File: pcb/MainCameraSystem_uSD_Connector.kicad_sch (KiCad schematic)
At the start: 10 parts, among them J3 0472192001

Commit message: Removed series resistors for `uSD Connector` design block.
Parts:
- removed R11, R12, R13, R14, R15, R16: R_Small, Resistor_SMD:R_1206_3216Metric_Pad1.30x1.75mm_HandSolder, symbol Device:R_Small
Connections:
- net clock: now also J3.5 (CLK)
- net cmd: now also J3.3 (CMD)
- net data_0: now also J3.7 (DAT0)
- net data_1: now also J3.8 (DAT1)
- net data_2: now also J3.1 (DAT2)
- net data_3: now also J3.2 (DAT3/CD)
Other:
- note added: "uSD Connector (V7 : Removed series resistor)."
- note removed: "uSD Connector (V6 : Hierarchical labels)."

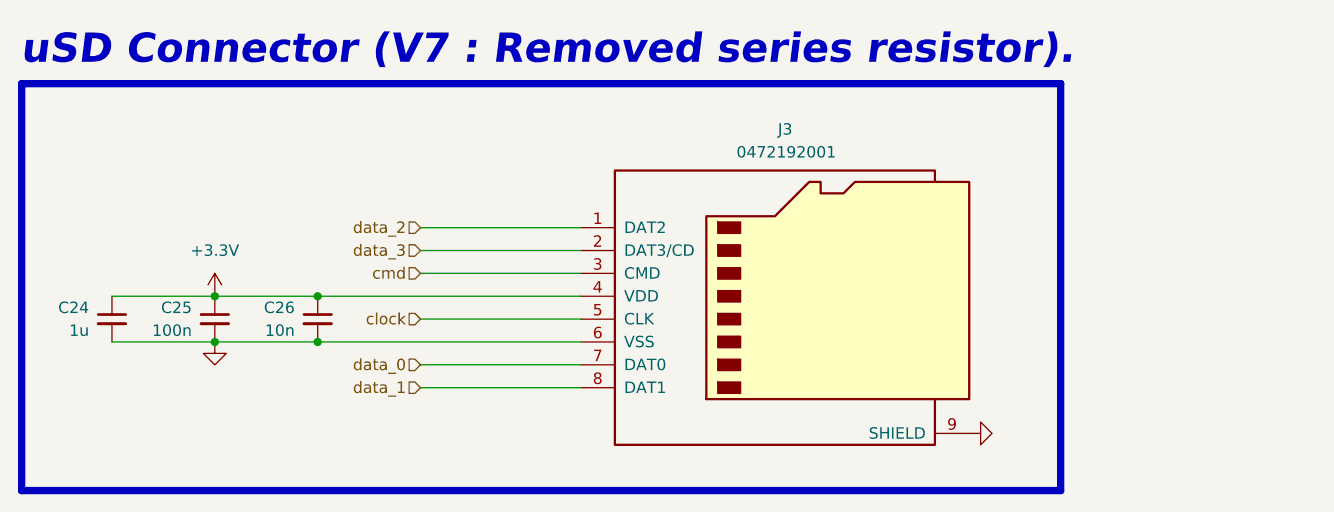
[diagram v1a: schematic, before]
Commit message: Fixing errata of missing pull-up resistors on `CMD` and `DAT0` lines of uSD connector.
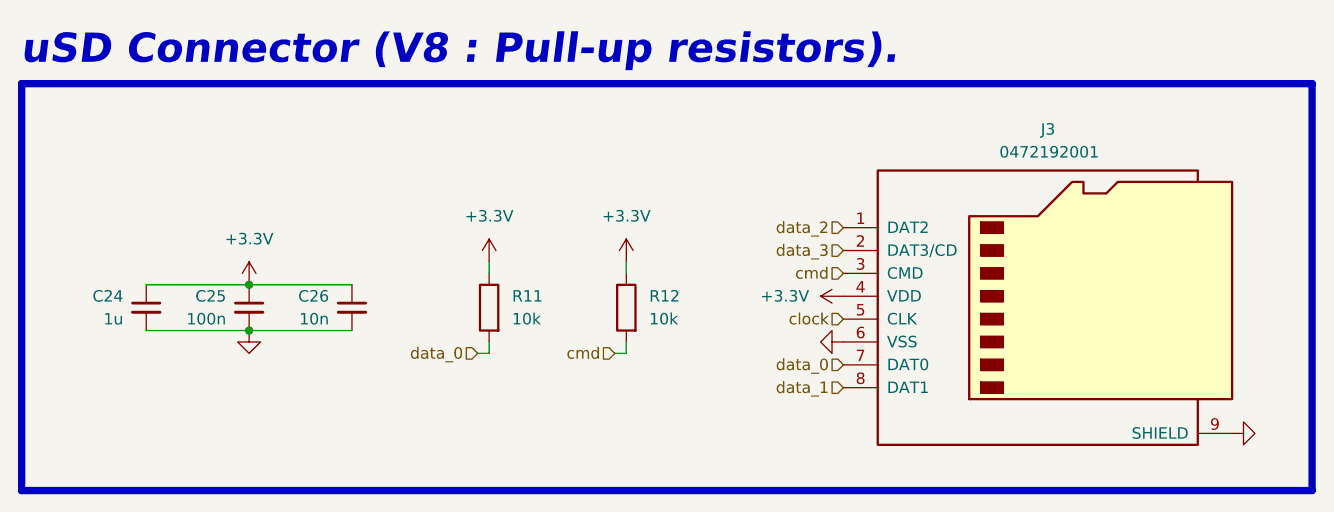
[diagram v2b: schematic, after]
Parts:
- added R11, R12: 10k, Resistor_SMD:R_1206_3216Metric_Pad1.30x1.75mm_HandSolder, symbol Device:R
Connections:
- net +3.3V: now also R11.1, R12.1
- net cmd: now also R12.2
- net data_0: now also R11.2
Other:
- note added: "uSD Connector (V8 : Pull-up resistors)."
- note removed: "uSD Connector (V7 : Removed series resistor)."
- moved on the sheet: C24, C25, C26, J3

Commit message: Laid out silkscreen and fixed schematic and PCB issues for `MainCameraSystem`.
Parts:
- renumbered C24 to C1, C25 to C2, C26 to C3, J3 to J4, R12 to R5, R11 to R6
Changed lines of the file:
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@@
 		(on_board yes)
 		(dnp no)
-		(property "Reference" "R12"
+		(property "Reference" "R5"
 			(at 114.3 77.4699 0)
 			(effects
@@
 			(project "MainCameraSystem"
 				(path "/caaf0100-eb77-4215-a2d5-ab172094720c/de6c6d71-2289-4145-9b43-d67662a46a31"
-					(reference "R12")
+					(reference "R5")
 					(unit 1)
 				)
@@
 		(on_board yes)
 		(dnp no)
-		(property "Reference" "C24"
+		(property "Reference" "C1"
 			(at 55.88 77.4762 0)
 			(effects
@@
 			(project "MainCameraSystem"
 				(path "/caaf0100-eb77-4215-a2d5-ab172094720c/de6c6d71-2289-4145-9b43-d67662a46a31"
-					(reference "C24")
+					(reference "C1")
 					(unit 1)
 				)
@@
 		(on_board yes)
 		(dnp no)
-		(property "Reference" "C25"
+		(property "Reference" "C2"
 			(at 67.31 77.4762 0)
 			(effects
@@
 			(project "MainCameraSystem"
 				(path "/caaf0100-eb77-4215-a2d5-ab172094720c/de6c6d71-2289-4145-9b43-d67662a46a31"
-					(reference "C25")
+					(reference "C2")
 					(unit 1)
 				)
@@
 		(on_board yes)
 		(dnp no)
-		(property "Reference" "J3"
+		(property "Reference" "J4"
 			(at 158.623 58.928 0)
 			(effects
@@
 			(project "MainCameraSystem"
 				(path "/caaf0100-eb77-4215-a2d5-ab172094720c/de6c6d71-2289-4145-9b43-d67662a46a31"
-					(reference "J3")
+					(reference "J4")
 					(unit 1)
 				)
@@
 		(on_board yes)
 		(dnp no)
-		(property "Reference" "R11"
+		(property "Reference" "R6"
 			(at 99.06 77.4699 0)
 			(effects
@@
 			(project "MainCameraSystem"
 				(path "/caaf0100-eb77-4215-a2d5-ab172094720c/de6c6d71-2289-4145-9b43-d67662a46a31"
-					(reference "R11")
+					(reference "R6")
 					(unit 1)
 				)
@@
 		(on_board yes)
 		(dnp no)
-		(property "Reference" "C26"
+		(property "Reference" "C3"
 			(at 78.74 77.4762 0)
 			(effects
@@
 			(project "MainCameraSystem"
 				(path "/caaf0100-eb77-4215-a2d5-ab172094720c/de6c6d71-2289-4145-9b43-d67662a46a31"
-					(reference "C26")
-					(unit 1)
-				)
+					(reference "C3")
+					(unit 1)
+				)

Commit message: Finalized `MCS-R1`.
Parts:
- renumbered R6 to R5, R5 to R6
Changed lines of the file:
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@@
 		(on_board yes)
 		(dnp no)
-		(property "Reference" "R5"
+		(property "Reference" "R6"
 			(at 114.3 77.4699 0)
 			(effects
@@
 			(project "MainCameraSystem"
 				(path "/caaf0100-eb77-4215-a2d5-ab172094720c/de6c6d71-2289-4145-9b43-d67662a46a31"
-					(reference "R5")
+					(reference "R6")
 					(unit 1)
 				)
@@
 		(on_board yes)
 		(dnp no)
-		(property "Reference" "R6"
+		(property "Reference" "R5"
 			(at 99.06 77.4699 0)
 			(effects
@@
 			(project "MainCameraSystem"
 				(path "/caaf0100-eb77-4215-a2d5-ab172094720c/de6c6d71-2289-4145-9b43-d67662a46a31"
-					(reference "R6")
-					(unit 1)
-				)
+					(reference "R5")
+					(unit 1)
+				)
